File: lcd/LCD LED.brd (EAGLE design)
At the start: 56.6 x 64 mm, 23 parts, among them T1 MMDT3904, U1 SX1509

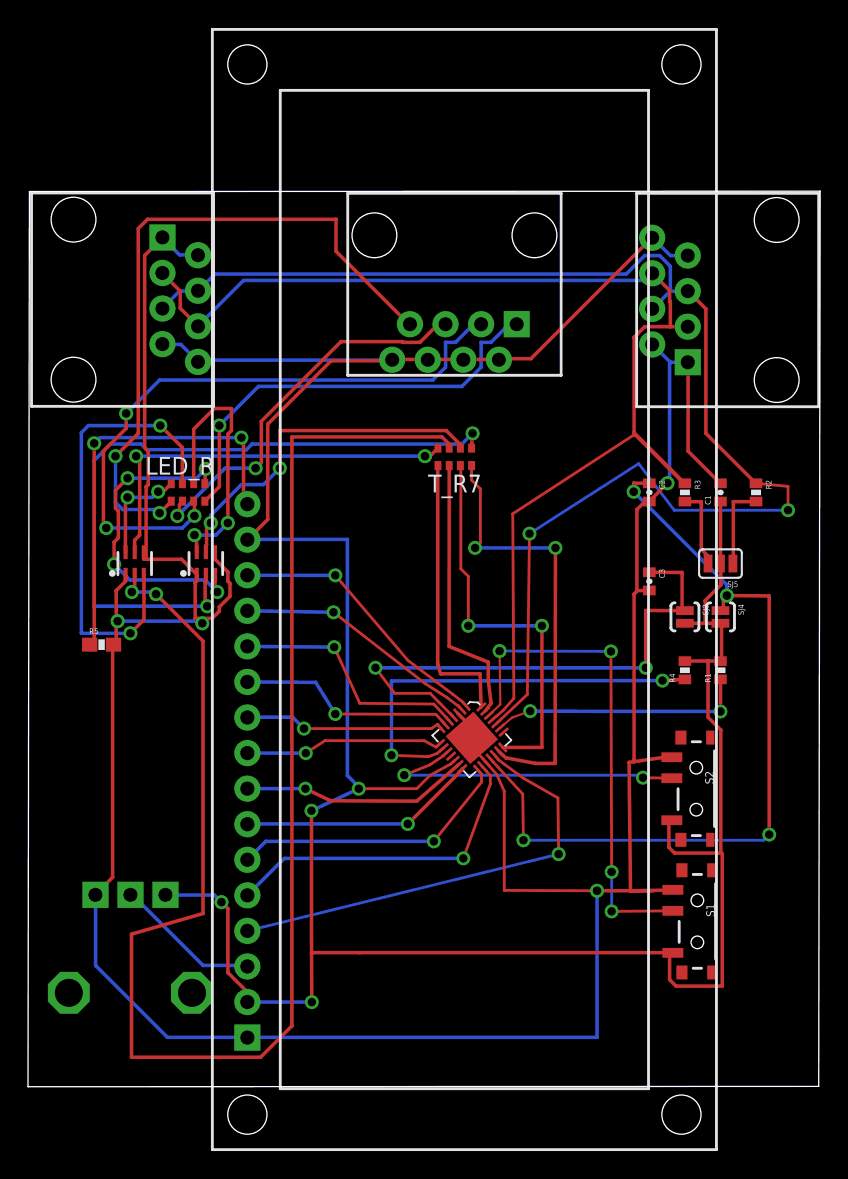
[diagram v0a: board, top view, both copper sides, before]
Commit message: added in changes to the lcd to use 4 wire interface updated other schematics to have cascading of interrupt
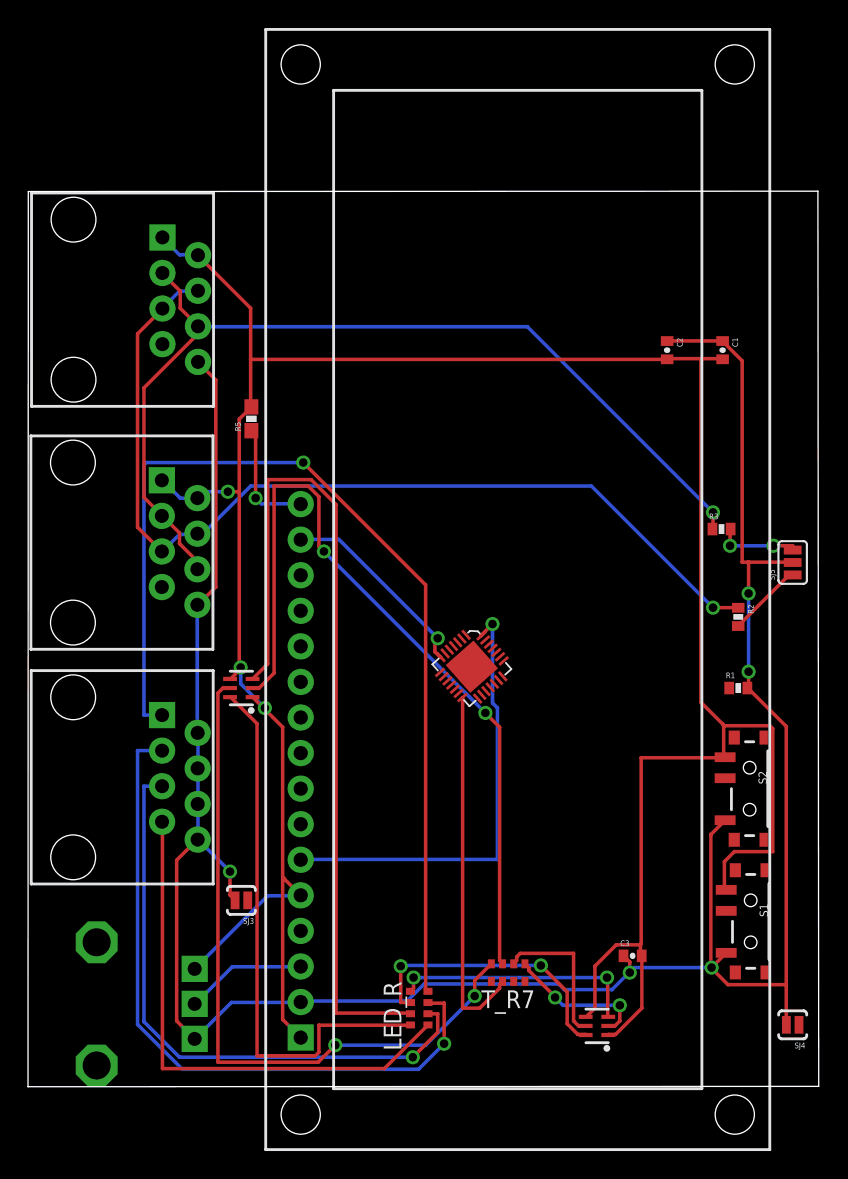
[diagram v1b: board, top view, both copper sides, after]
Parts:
- removed R4: 10k, SparkFun-Passives:0402-RES
- removed RV2: (no value), SparkFun-Electromechanical:ALPS_POT
- added CONTRAST: (no value), SparkFun-Electromechanical:ALPS_POT
- moved I2COUT 53.2 mm to (5.75, 75.2), turned to 270 degrees
- moved CUSOM_LED1 47.3 mm to (5.77, 58.4), turned to 270 degrees
- moved U$4 43.3 mm to (43.2, 40.6), turned to 90 degrees
- moved LED_R 40.4 mm to (30.5, 41.9), turned to 270 degrees
- moved SJ3 37.6 mm to (17.8, 49.6), turned to 180 degrees
- moved T_R7 37.0 mm to (36.8, 44.5)
- moved SJ4 29.6 mm to (57.1, 40.7), turned to 180 degrees
- moved C3 26.8 mm to (45.7, 45.6), turned to 0 degrees
- moved R5 19.4 mm to (18.5, 84.0), turned to 90 degrees
- moved T1 11.7 mm to (17.8, 64.8), turned to 90 degrees
- moved C2 10.2 mm to (48.2, 88.9)
- moved C1 10.2 mm to (52.1, 88.9), turned to 270 degrees
- moved R2 8.98 mm to (53.3, 69.8)
- moved SJ5 5.16 mm to (57.1, 73.7), turned to 90 degrees
- moved U1 5.08 mm to (34.2, 66.3)
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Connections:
- net 15 renamed IO15
- removed net 0: T_R7.1, U1.28
- removed net 1: T_R7.2, U1.27
- removed net 10: LCD1.12, U1.5
- removed net 11: LCD1.13, U1.2
- removed net 12: LCD1.14, U1.1
- removed net 13: T_R7.3, U1.21
- removed net 14: T_R7.4, U1.20
- removed net 2: LCD1.4, U1.19
- removed net 3: LCD1.5, U1.16
- removed net 4: LCD1.6, U1.15
- removed net 5: LCD1.7, U1.14
- removed net 6: LCD1.8, U1.13
- removed net 7: LCD1.9, U1.8
- removed net 8: LCD1.10, U1.7
- removed net 9: LCD1.11, U1.6
- removed net NINT: R4.1, U1.9
- removed net VO: LCD1.3, RV2.P$2
- new net INTERRUPT_EXTERNAL: I2CIN.7, U1.20
- new net INTERRUPT_INTERNAL: I2COUT.7, U1.19, U1.9
- new net IO14: U1.21
- new net IO7: U1.8
- new net LCD_BACKLIGHT: LCD1.15, U1.7
- new net LCD_CONTRAST: CONTRAST.P$2, LCD1.3
- new net LCD_D0: LCD1.7
- new net LCD_D1: LCD1.8
- new net LCD_D2: LCD1.9
- new net LCD_D3: LCD1.10
- new net LCD_D4: LCD1.11, U1.1
- new net LCD_D5: LCD1.12, U1.2
- new net LCD_D6: LCD1.13, U1.5
- new net LCD_D7: LCD1.14, U1.6
- new net LCD_E: LCD1.6, U1.28
- new net LCD_RS: LCD1.4, U1.27
- new net LED_1: T_R7.1, U1.13
- new net LED_2: T_R7.2, U1.14
- new net LED_3: T_R7.3, U1.15
- new net LED_4: T_R7.4, U1.16
- net 3.3V: now also C2.1, C3.1, CONTRAST.P$1; no longer I2CIN.7, I2COUT.7, LCD1.15, R4.2, RV2.P$1
- net GND: now also CONTRAST.P$3, LCD1.5; no longer RV2.P$3
- net VCC1: no longer C3.1
- net VCC2: no longer C2.1
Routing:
- net VCC2: track 57.8 -> 0.00 mm, vias 4 -> 0
- net G2: track 107.6 -> 57.6 mm
- net N$8: track 31.1 -> 72.1 mm
- net G4: track 50.1 -> 10.2 mm
- net VCC1: track 38.6 -> 0.00 mm, vias 2 -> 0
- net ADDR0: track 35.8 -> 0.00 mm, vias 4 -> 0
- net 3.3V: track 207.6 -> 173.4 mm, vias 4 -> 5
- net 2: track 32.4 -> 0.00 mm, vias 1 -> 0
- net LCD_E: track 0.00 -> 32.2 mm, vias 0 -> 1
- net 14: track 31.9 -> 0.00 mm, vias 2 -> 0
- net N$16: track 7.57 -> 39.4 mm, vias 2 -> 0
- net SDA: track 98.9 -> 68.6 mm, vias 2 -> 1
- net NINT: track 30.2 -> 0.00 mm, vias 2 -> 0
- net N$15: track 33.1 -> 62.0 mm, vias 2 -> 0
- net 13: track 28.4 -> 0.00 mm, vias 2 -> 0
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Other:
- board size 56.6 x 64 mm -> 56.5 x 64 mm
